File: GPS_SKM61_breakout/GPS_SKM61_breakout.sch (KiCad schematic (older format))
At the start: 2 parts, among them P1 CONN_01X06, U1 SKM61

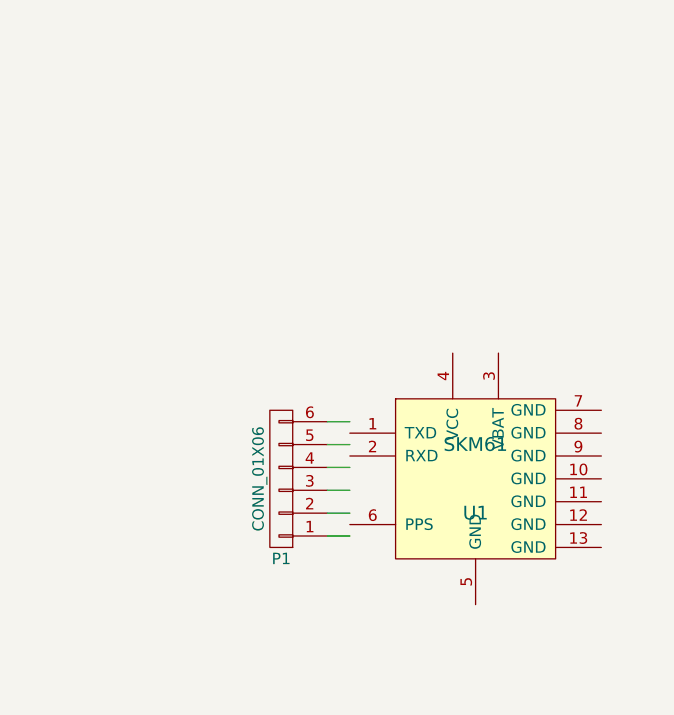
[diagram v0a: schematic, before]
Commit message: added a few more breakout board projects
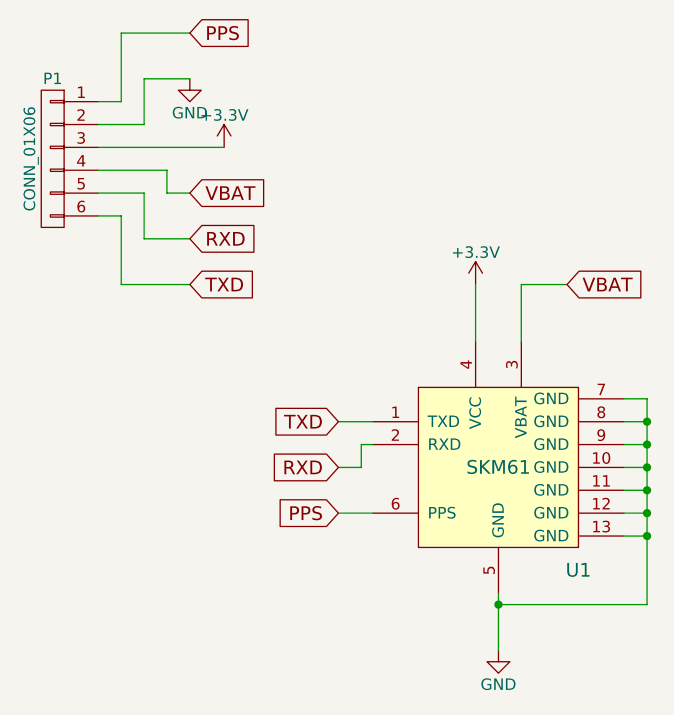
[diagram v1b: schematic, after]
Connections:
- net labels added: +3.3V, GND, PPS, RXD, TXD, VBAT
- wire segments 6 -> 34
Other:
- moved on the sheet: P1, U1
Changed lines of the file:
@@
 L SKM61 U1
 U 1 1 5797F602
-P 5900 3750
-F 0 "U1" H 5900 3600 60  0000 C CNN
-F 1 "SKM61" H 5900 3900 60  0000 C CNN
-F 2 "scintilla:SKM61" H 5900 3750 60  0001 C CNN
-F 3 "" H 5900 3750 60  0000 C CNN
-	1    5900 3750
+P 6000 3700
+F 0 "U1" H 6350 3250 60  0000 C CNN
+F 1 "SKM61" H 6000 3700 60  0000 C CNN
+F 2 "scintilla:SKM61" H 6000 3700 60  0001 C CNN
+F 3 "" H 6000 3700 60  0000 C CNN
+	1    6000 3700
+	1    0    0    -1
+$EndComp
+$Comp
+L CONN_01X06 P1
+U 1 1 57980387
+P 4050 2350
+F 0 "P1" H 4050 2700 50  0000 C CNN
+F 1 "CONN_01X06" V 4150 2350 50  0000 C CNN
+F 2 "Pin_Headers:Pin_Header_Straight_1x06" H 4050 2350 50  0001 C CNN
+F 3 "" H 4050 2350 50  0000 C CNN
+	1    4050 2350
+	-1   0    0    -1
+$EndComp
+$Comp
+L GND #PWR01
+U 1 1 579AA8C3
+P 6000 4500
+F 0 "#PWR01" H 6000 4250 50  0001 C CNN
+F 1 "GND" H 6000 4350 50  0000 C CNN
+F 2 "" H 6000 4500 50  0000 C CNN
+F 3 "" H 6000 4500 50  0000 C CNN
+	1    6000 4500
+	1    0    0    -1
+$EndComp
+Text GLabel 5300 3500 0    60   Input ~ 0
+TXD
+Text GLabel 4650 2900 2    60   Input ~ 0
+TXD
+$Comp
+L +3.3V #PWR02
+U 1 1 579AA966
+P 5900 2900
+F 0 "#PWR02" H 5900 2750 50  0001 C CNN
+F 1 "+3.3V" H 5900 3040 50  0000 C CNN
+F 2 "" H 5900 2900 50  0000 C CNN
+F 3 "" H 5900 2900 50  0000 C CNN
+	1    5900 2900
 	1    0    0    -1
 $EndComp
 Wire Wire Line
-	5350 3500 5250 3500
+	6000 4500 6000 4250
 Wire Wire Line
-	5350 3600 5250 3600
+	5300 3500 5450 3500
 Wire Wire Line
-	5350 3700 5250 3700
+	5900 2900 5900 3150
 Wire Wire Line
-	5350 3800 5250 3800
+	5450 3600 5400 3600
 Wire Wire Line
-	5350 3900 5250 3900
+	5400 3600 5400 3700
 Wire Wire Line
-	5350 4000 5250 4000
+	5400 3700 5300 3700
+Wire Wire Line
+	4350 2100 4250 2100
+Wire Wire Line
+	4350 1800 4350 2100
+Wire Wire Line
+	4250 2200 4450 2200
+Wire Wire Line
+	4450 2200 4450 2000
+Wire Wire Line
+	4450 2000 4650 2000
+Wire Wire Line
+	4350 1800 4650 1800
+Wire Wire Line
+	4250 2300 4800 2300
+Wire Wire Line
+	4250 2400 4550 2400
+Wire Wire Line
+	4550 2400 4550 2500
+Wire Wire Line
+	4550 2500 4650 2500
+Wire Wire Line
+	4250 2500 4450 2500
+Wire Wire Line
+	4450 2500 4450 2700
+Wire Wire Line
+	4450 2700 4650 2700
+Wire Wire Line
+	4250 2600 4350 2600
+Wire Wire Line
+	4350 2600 4350 2900
+Wire Wire Line
+	4350 2900 4650 2900
+Text GLabel 4650 2700 2    60   Input ~ 0
+RXD
+Text GLabel 5300 3700 0    60   Input ~ 0
+RXD
+Wire Wire Line
+	5450 3900 5300 3900
+Text GLabel 5300 3900 0    60   Input ~ 0
+PPS
+Wire Wire Line
+	6550 3400 6650 3400
+Wire Wire Line
+	6650 3400 6650 4300
+Wire Wire Line
+	6550 4000 6650 4000
+Connection ~ 6650 4000
+Wire Wire Line
+	6550 3900 6650 3900
+Connection ~ 6650 3900
+Wire Wire Line
+	6550 3800 6650 3800
+Connection ~ 6650 3800
+Wire Wire Line
+	6550 3700 6650 3700
+Connection ~ 6650 3700
+Wire Wire Line
+	6550 3600 6650 3600
+Connection ~ 6650 3600
+Wire Wire Line
+	6550 3500 6650 3500
+Connection ~ 6650 3500
+Wire Wire Line
+	6650 4300 6000 4300
+Connection ~ 6000 4300
+Wire Wire Line
+	6100 3150 6100 2900
+Wire Wire Line
+	6100 2900 6300 2900
+Text GLabel 6300 2900 2    60   Input ~ 0
+VBAT
 $Comp
-L CONN_01X06 P1
-U 1 1 57980387
-P 5050 3750
-F 0 "P1" H 5050 4100 50  0000 C CNN
-F 1 "CONN_01X06" V 5150 3750 50  0000 C CNN
-F 2 "Pin_Headers:Pin_Header_Straight_1x06" H 5050 3750 50  0001 C CNN
-F 3 "" H 5050 3750 50  0000 C CNN
-	1    5050 3750
-	-1   0    0    1
+L +3.3V #PWR03
+U 1 1 579AAD35
+P 4800 2300
+F 0 "#PWR03" H 4800 2150 50  0001 C CNN
+F 1 "+3.3V" H 4800 2440 50  0000 C CNN
+F 2 "" H 4800 2300 50  0000 C CNN
+F 3 "" H 4800 2300 50  0000 C CNN
+	1    4800 2300
+	1    0    0    -1
+$EndComp
+Text GLabel 4650 2500 2    60   Input ~ 0
+VBAT
+Text GLabel 4650 1800 2    60   Input ~ 0
+PPS
+$Comp
+L GND #PWR?
+U 1 1 579AAE93
+P 4650 2000
+F 0 "#PWR?" H 4650 1750 50  0001 C CNN
+F 1 "GND" H 4650 1850 50  0000 C CNN
+F 2 "" H 4650 2000 50  0000 C CNN
+F 3 "" H 4650 2000 50  0000 C CNN
+	1    4650 2000
+	1    0    0    -1
 $EndComp
 $EndSCHEMATC
